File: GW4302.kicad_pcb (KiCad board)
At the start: 4 copper layers, 57.9 x 51.6 mm, 29 parts, among them J1 C64

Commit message: As submitted to JLC
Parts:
- removed the H1 at (107.7, 47.5)
- removed the H2 at (156.5, 47.5)
- removed REF**: SOT-223, stdpads:SOT-223
- removed REF** (x7): C_0603, stdpads:C_0603
- removed REF**: TSSOP-14_4.4x5mm_P0.65mm, stdpads:TSSOP-14_4.4x5mm_P0.65mm
- removed REF**: TQFP-100_14x14mm_P0.5mm, stdpads:TQFP-100_14x14mm_P0.5mm
- removed REF** (x2): TSSOP-20_4.4x6.5mm_P0.65mm, stdpads:TSSOP-20_4.4x6.5mm_P0.65mm
- added C1: 10u, stdpads:C_0805, F.Cu at (109.5, 74.8)
- added C10: 2u2, stdpads:C_0603, F.Cu at (131.3, 79.8)
- added C12: 2u2, stdpads:C_0603, F.Cu at (149.8, 79.8)
- added C13: 2u2, stdpads:C_0603, F.Cu at (112.3, 61.5)
- added C14: 2u2, stdpads:C_0603, F.Cu at (112.3, 70.0)
- added C15: 2u2, stdpads:C_0603, F.Cu at (116.5, 75.0)
- added C16: 2u2, stdpads:C_0603, F.Cu at (125.5, 75.0)
- added C17: 2u2, stdpads:C_0603, F.Cu at (128.8, 75.0)
- added C18: 2u2, stdpads:C_0603, F.Cu at (131.7, 69.0)
- added C19: 2u2, stdpads:C_0603, F.Cu at (131.7, 60.5)
- added C2: 10u, stdpads:C_0805, F.Cu at (112.6, 73.4)
- added C20: 2u2, stdpads:C_0603, F.Cu at (126.2, 55.6)
- added C21: 2u2, stdpads:C_0603, F.Cu at (119.8, 55.6)
- added C22: 2u2, stdpads:C_0603, F.Cu at (115.2, 55.6)
- added C23: 2u2, stdpads:C_0603, F.Cu at (115.8, 79.5)
- added C24: 2u2, stdpads:C_0603, F.Cu at (156.8, 72.0)
- added C25: 2u2, stdpads:C_0603, F.Cu at (156.8, 68.8)
- added C26: 2u2, stdpads:C_0603, F.Cu at (156.8, 64.8)
- added C27: 2u2, stdpads:C_0603, F.Cu at (156.8, 54.4)
- added C28: 2u2, stdpads:C_0603, F.Cu at (141.2, 64.8)
- added C29: 2u2, stdpads:C_0603, F.Cu at (141.2, 71.2)
- added C3: 10u, stdpads:C_0805, F.Cu at (106.2, 62.1)
- added C30: 2u2, stdpads:C_0603, F.Cu at (110.2, 47.0)
- added C31: 2u2, stdpads:C_0603, F.Cu at (116.7, 40.8)
- added C32: 22p, stdpads:C_0603, F.Cu at (110.0, 56.5)
- added C33: 22p, stdpads:C_0603, F.Cu at (107.4, 44.0)
- added C34: 22p, stdpads:C_0603, F.Cu at (141.4, 41.2)
- added C35: 2u2, stdpads:C_0603, F.Cu at (119.6, 41.7)
- added C36: 2u2, stdpads:C_0603, F.Cu at (146.7, 40.6)
- added C37: 2u2, stdpads:C_0603, F.Cu at (148.0, 48.6)
- added C38: 22p, stdpads:C_0603, F.Cu at (129.2, 44.8)
- added C39: 22p, stdpads:C_0603, F.Cu at (111.8, 39.3)
- added C4: 10u, stdpads:C_0805, F.Cu at (109.7, 62.1)
- added C5: 10u, stdpads:C_0805, F.Cu at (106.2, 59.9)
- added C6: 10u, stdpads:C_0805, F.Cu at (109.7, 59.9)
- added C7: 22p, stdpads:C_0603, F.Cu at (148.0, 45.6)
- added H3: , stdpads:PasteHole_1.152mm_NPTH, F.Cu at (156.5, 38.7)
- added H4: , stdpads:PasteHole_1.152mm_NPTH, F.Cu at (105.1, 41.3)
- added H5: , stdpads:PasteHole_1.152mm_NPTH, F.Cu at (158.8, 82.9)
- added J2: microUSB, stdpads:USB_Micro-B_ShouHan_MicroXNJ, F.Cu at (134.3, 39.8)
- added J3: JTAG, Connector:Tag-Connect_TC2050-IDC-FP_2x05_P1.27mm_Vertical, F.Cu at (154.7, 47.4)
- added R1: 1k, stdpads:R_0603, F.Cu at (121.7, 41.6)
- added R10: 47, stdpads:R_0603, F.Cu at (145.8, 46.4)
- added R11: 10k, stdpads:R_0603, F.Cu at (137.4, 56.0)
- added R12: 10k, stdpads:R_0603, F.Cu at (137.4, 54.5)
- added R13: 10k, stdpads:R_0603, F.Cu at (148.0, 47.1)
- added R14: 10k, stdpads:R_0603, F.Cu at (137.4, 53.0)
- added R15: 10k, stdpads:R_0603, F.Cu at (111.8, 40.9)
- added R16: 1k, stdpads:R_0603, F.Cu at (139.9, 41.2)
- added R2: 1k, stdpads:R_0603, F.Cu at (136.4, 44.4)
- added R3: 47, stdpads:R_0603, F.Cu at (144.9, 43.2)
- added R4: 10k, stdpads:R_0603, F.Cu at (108.3, 40.9)
- added R5: 1k, stdpads:R_0603, F.Cu at (115.8, 82.3)
- added R6: 47, stdpads:R_0603, F.Cu at (119.4, 75.8)
- added R7: 47, stdpads:R_0603, F.Cu at (119.4, 77.3)
- added R8: 10k, stdpads:R_0603, F.Cu at (141.2, 53.6)
- added R9: 10k, stdpads:R_0603, F.Cu at (137.4, 57.5)
- added U10: 74AHC125PW, stdpads:TSSOP-14_4.4x5mm_P0.65mm, F.Cu at (125.8, 43.5)
- added U11: 74LVC1G04GW, stdpads:SOT-353, F.Cu at (120.7, 45.0)
- added U12: 74LVC1G04GW, stdpads:SOT-353, F.Cu at (144.1, 40.5)
- added U13: CH340G, stdpads:SOIC-16_3.9mm, F.Cu at (114.9, 46.9)
- added U2: 74AHC245PW, stdpads:TSSOP-20_4.4x6.5mm_P0.65mm, F.Cu at (135.8, 82.0)
- added U3: LD1117S33, stdpads:SOT-223, F.Cu at (108.0, 69.1)
- added U5: 74AHC245PW, stdpads:TSSOP-20_4.4x6.5mm_P0.65mm, F.Cu at (124.8, 82.0)
- added U8: LCMXO2-640-TG100, stdpads:TQFP-100_14x14mm_P0.5mm, F.Cu at (122.0, 65.3)
- added Y1: 12M, stdpads:Crystal_HC49-SMD, F.Cu at (106.7, 51.5)
- C11, C8, C9: renamed from REF**; value C_0603 -> 2u2
- U1, U4: renamed from REF**; value TSSOP-20_4.4x6.5mm_P0.65mm -> 74AHC245PW
- U6: renamed from REF**; value TSSOP-14_4.4x5mm_P0.65mm -> 74AHC125PW
- U7: renamed from REF**; value SOT-353 -> 74LVC1G04GW
- U9: renamed from REF**; value TSOP-II-54_22.2x10.16mm_P0.8mm -> W9825G6KH-6
- moved U7 18.2 mm to (118.0, 79.7)
- moved FID1 8.76 mm to (105.1, 38.7)
- moved FID2 8.76 mm to (159.1, 38.7)
- moved C8 6.35 mm to (108.5, 79.8)
- moved U6 6.35 mm to (112.0, 82.0)
- moved FID3 2.54 mm to (158.8, 85.5)
- moved C9 1.75 mm to (120.4, 79.8)
- turned U9 to 90 degrees
- renumbered H4 to H1, H3 to H2
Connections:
- C11 pad 1: (no net) -> +3V3
- C11 pad 2: (no net) -> GND
- C8 pad 1: (no net) -> +3V3
- C8 pad 2: (no net) -> GND
- C9 pad 1: (no net) -> +3V3
- C9 pad 2: (no net) -> GND
- U1 pad 1: (no net) -> /ADIR
- U1 pad 10: (no net) -> GND
- U1 pad 11: (no net) -> /BA0
- U1 pad 12: (no net) -> /BA1
- U1 pad 13: (no net) -> /BA2
- U1 pad 14: (no net) -> /BA3
- U1 pad 15: (no net) -> /BA4
- U1 pad 16: (no net) -> /BA5
- U1 pad 17: (no net) -> /BA6
- U1 pad 18: (no net) -> /BA7
- U1 pad 19: (no net) -> /A~OE~
- U1 pad 2: (no net) -> /A7
- U1 pad 20: (no net) -> +3V3
- U1 pad 3: (no net) -> /A6
- U1 pad 4: (no net) -> /A5
- U1 pad 5: (no net) -> /A4
- U1 pad 6: (no net) -> /A3
- U1 pad 7: (no net) -> /A2
- U1 pad 8: (no net) -> /A1
- U1 pad 9: (no net) -> /A0
- U4 pad 1: (no net) -> /DDIR
- U4 pad 10: (no net) -> GND
- U4 pad 11: (no net) -> /BD0
- U4 pad 12: (no net) -> /BD1
- U4 pad 13: (no net) -> /BD2
- U4 pad 14: (no net) -> /BD3
- U4 pad 15: (no net) -> /BD4
- U4 pad 16: (no net) -> /BD5
- U4 pad 17: (no net) -> /BD6
- U4 pad 18: (no net) -> /BD7
- U4 pad 19: (no net) -> /D~OE~
- U4 pad 2: (no net) -> /D7
- U4 pad 20: (no net) -> +3V3
- U4 pad 3: (no net) -> /D6
- U4 pad 4: (no net) -> /D5
- U4 pad 5: (no net) -> /D4
- U4 pad 6: (no net) -> /D3
- U4 pad 7: (no net) -> /D2
- U4 pad 8: (no net) -> /D1
- U4 pad 9: (no net) -> /D0
- U6 pad 1: (no net) -> GND
- U6 pad 10: (no net) -> /DMA~OE~
- U6 pad 11: (no net) -> /~IRQ~
- U6 pad 12: (no net) -> GND
- U6 pad 13: (no net) -> /IRQ~OE~
- U6 pad 14: (no net) -> +3V3
- U6 pad 2: (no net) -> GND
- U6 pad 3: (no net) -> Net-(U6-Pad3)
- U6 pad 4: (no net) -> /RW~OE~
- U6 pad 5: (no net) -> /DMAR~W~
- U6 pad 6: (no net) -> /R~W~
- U6 pad 7: (no net) -> GND
- U6 pad 8: (no net) -> /~DMA~
- U6 pad 9: (no net) -> GND
- U7 pad 1: (no net) -> Net-(U7-Pad1)
- U7 pad 2: (no net) -> /DotClk
- U7 pad 3: (no net) -> GND
- U7 pad 4: (no net) -> Net-(R6-Pad2)
- U7 pad 5: (no net) -> +3V3
- U9 pad 1: (no net) -> +3V3
- U9 pad 10: (no net) -> /RD5
- U9 pad 11: (no net) -> /RD6
- U9 pad 12: (no net) -> GND
- U9 pad 13: (no net) -> /RD7
- U9 pad 14: (no net) -> +3V3
- U9 pad 15: (no net) -> /RDQML
- U9 pad 16: (no net) -> /R~WE~
- U9 pad 17: (no net) -> /~CAS~
- U9 pad 18: (no net) -> /~RAS~
- U9 pad 19: (no net) -> /R~CS~
- U9 pad 2: (no net) -> /RD0
- U9 pad 20: (no net) -> /RBA0
- U9 pad 21: (no net) -> /RBA1
- U9 pad 22: (no net) -> /RA10
- U9 pad 23: (no net) -> /RA0
- U9 pad 24: (no net) -> /RA1
- U9 pad 25: (no net) -> /RA2
- U9 pad 26: (no net) -> /RA3
- U9 pad 27: (no net) -> +3V3
- U9 pad 28: (no net) -> GND
- U9 pad 29: (no net) -> /RA4
- U9 pad 3: (no net) -> +3V3
- U9 pad 30: (no net) -> /RA5
- U9 pad 31: (no net) -> /RA6
- U9 pad 32: (no net) -> /RA7
- U9 pad 33: (no net) -> /RA8
- U9 pad 34: (no net) -> /RA9
- U9 pad 35: (no net) -> /RA11
- U9 pad 36: (no net) -> /RA12
- U9 pad 37: (no net) -> /RCKE
- U9 pad 38: (no net) -> /RCLK
- U9 pad 39: (no net) -> /RDQMH
- U9 pad 4: (no net) -> /RD1
- U9 pad 41: (no net) -> GND
- U9 pad 42: (no net) -> /RD7
- U9 pad 43: (no net) -> +3V3
- U9 pad 44: (no net) -> /RD6
- U9 pad 45: (no net) -> /RD5
- U9 pad 46: (no net) -> GND
- U9 pad 47: (no net) -> /RD4
- U9 pad 48: (no net) -> /RD3
- U9 pad 49: (no net) -> +3V3
- U9 pad 5: (no net) -> /RD2
- U9 pad 50: (no net) -> /RD2
- U9 pad 51: (no net) -> /RD1
- U9 pad 52: (no net) -> GND
- U9 pad 53: (no net) -> /RD0
- U9 pad 54: (no net) -> GND
- U9 pad 6: (no net) -> GND
- U9 pad 7: (no net) -> /RD3
- U9 pad 8: (no net) -> /RD4
- U9 pad 9: (no net) -> +3V3
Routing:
- net +3V3: track 0.00 -> 387.7 mm, vias 0 -> 122
- net GND: track 23.2 -> 166.8 mm, vias 48 -> 207
- net /TDO: track 0.00 -> 64.8 mm, vias 0 -> 3
- net /BD1: track 0.00 -> 59.3 mm, vias 0 -> 2
- net /BD0: track 0.00 -> 58.0 mm, vias 0 -> 2
- net /BD3: track 0.00 -> 58.0 mm, vias 0 -> 2
- net /TMS: track 0.00 -> 57.9 mm, vias 0 -> 4
- net /BD5: track 0.00 -> 56.6 mm, vias 0 -> 2
- net /BD2: track 0.00 -> 56.3 mm, vias 0 -> 2
- net /DDIR: track 0.00 -> 56.0 mm, vias 0 -> 2
- net /D~OE~: track 0.00 -> 56.0 mm, vias 0 -> 2
- net /BD4: track 0.00 -> 55.7 mm, vias 0 -> 2
- net /RA3: track 0.00 -> 55.5 mm
- net /BD7: track 0.00 -> 55.3 mm, vias 0 -> 2
- net /RA2: track 0.00 -> 54.6 mm
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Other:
- board size 57.9 x 51.6 mm -> 57.9 x 60.3 mm
- board text added: "JLCJLCJLCJLC"

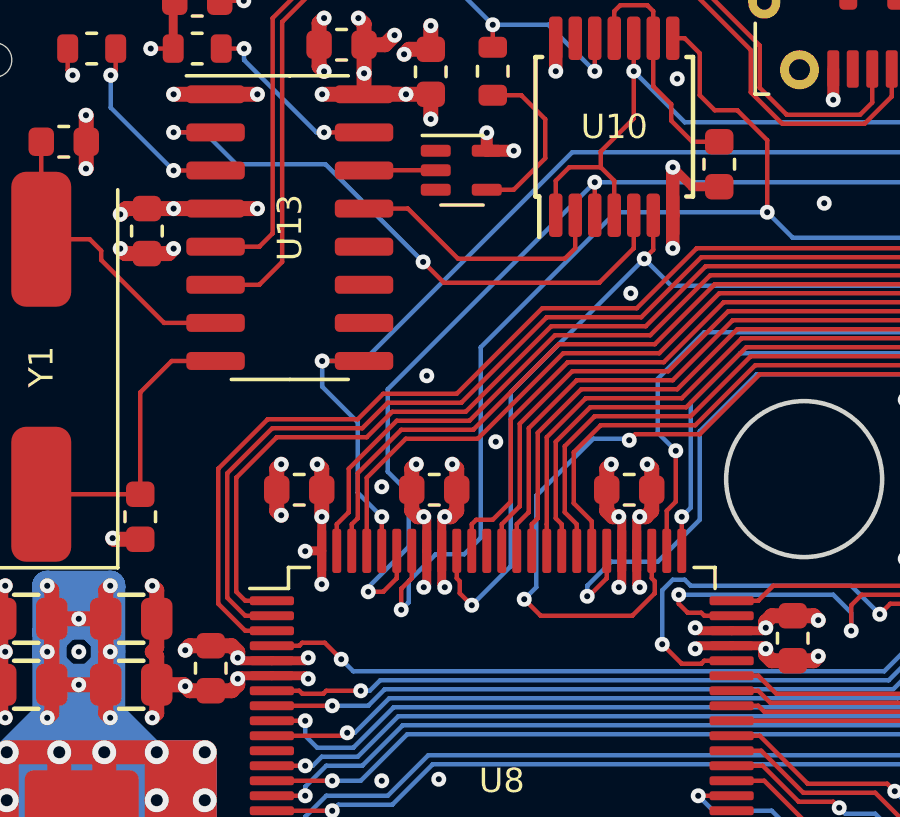
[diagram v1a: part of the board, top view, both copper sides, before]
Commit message: Fix JTAG connections on board
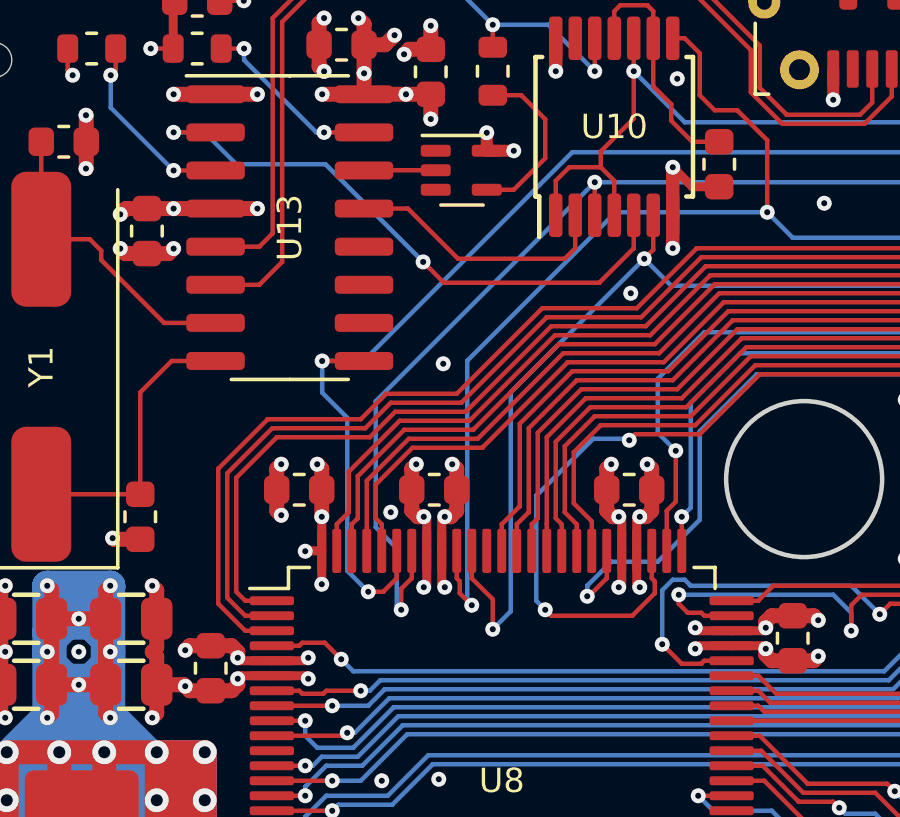
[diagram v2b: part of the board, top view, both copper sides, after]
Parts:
- U11, U12: value 74LVC1G04GW -> 74AHC1G04GW
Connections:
- U8 pad 28: Net-(U8-Pad28) -> /B~RESET~
- U8 pad 90: /RBA0 -> /TMS
- U8 pad 91: /TMS -> /TCKr
- U8 pad 94: /TCKr -> /TDI
- U8 pad 95: /TDI -> /TDO
- U8 pad 96: /TDO -> /RBA0
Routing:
- net /TDO: track 64.8 -> 68.0 mm
- net /RBA0: track 44.2 -> 46.6 mm
- net /TCKr: track 49.9 -> 48.3 mm
- net /TMS: track 57.9 -> 59.3 mm
- net /RA5: track 34.2 -> 33.6 mm
- net GND: vias 207 -> 206

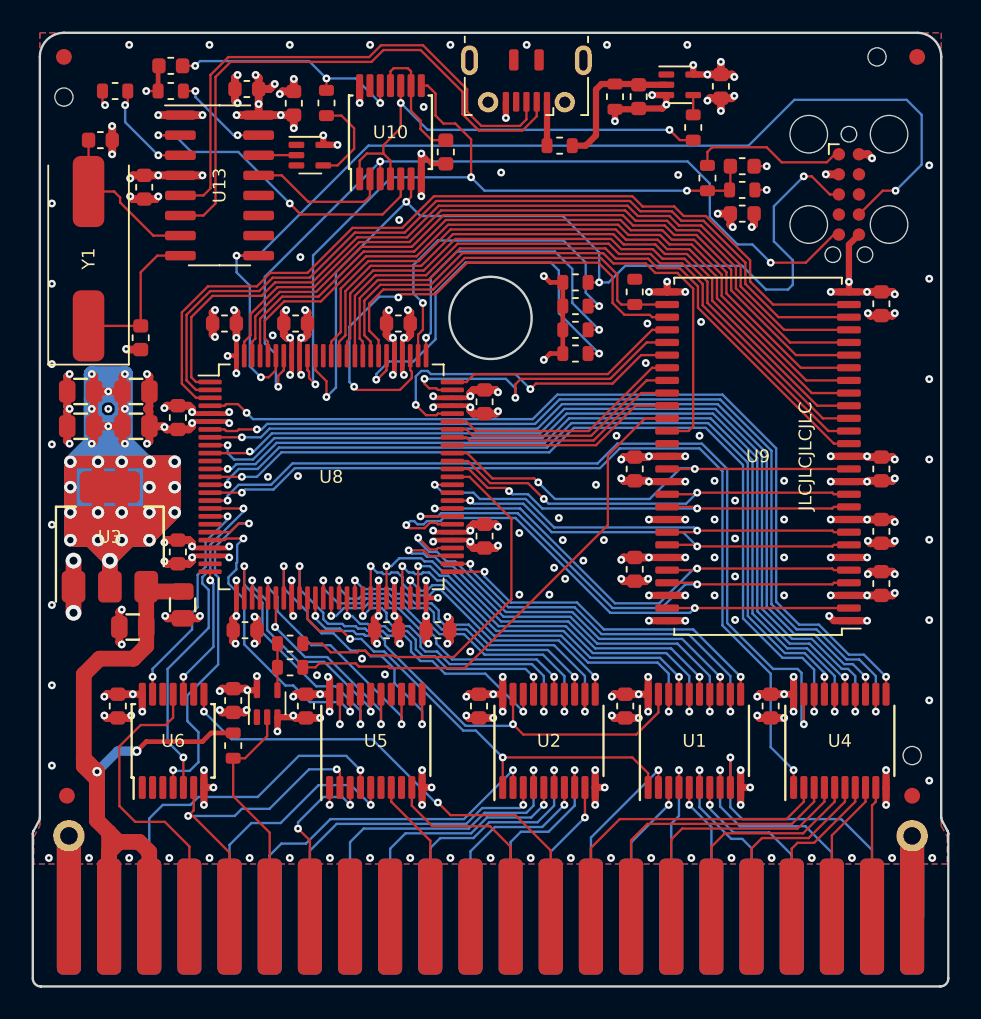
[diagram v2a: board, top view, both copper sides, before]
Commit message: Migrate to KiCAD 6
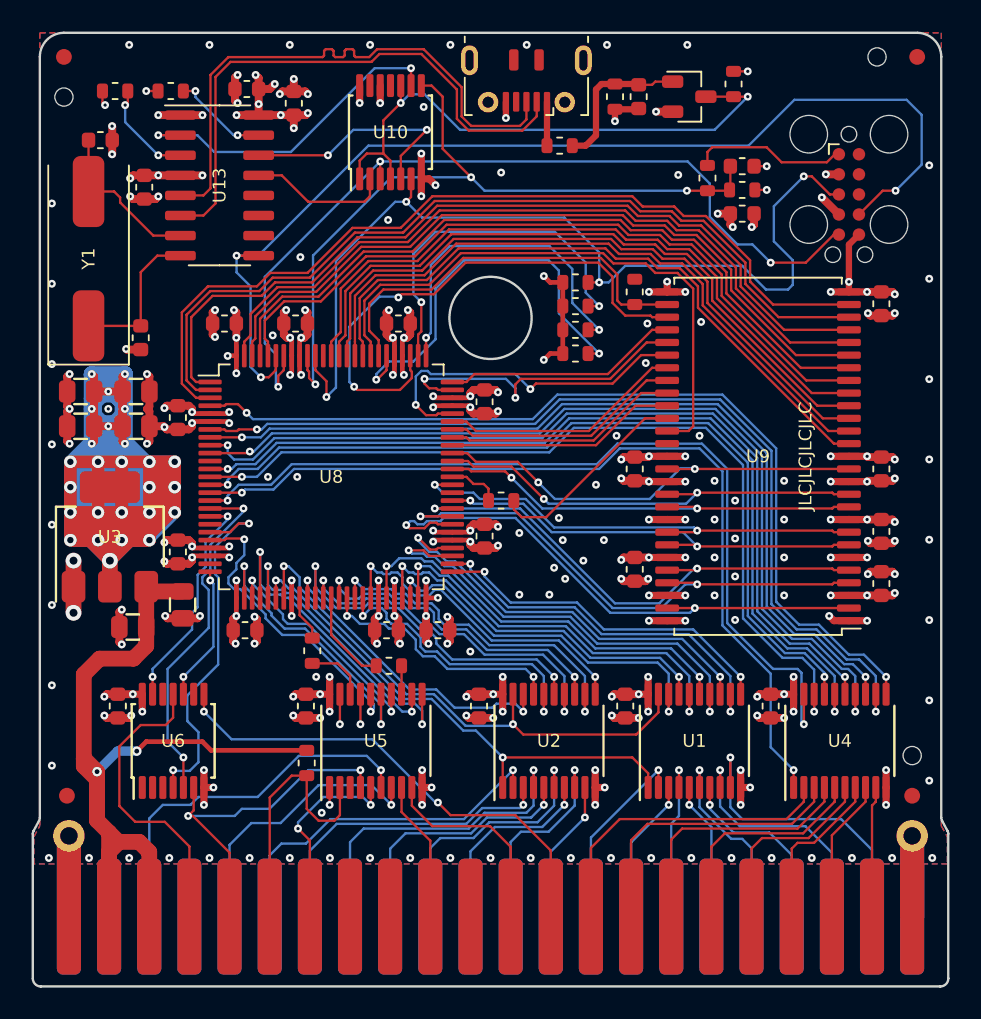
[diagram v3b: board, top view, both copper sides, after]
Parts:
- removed the C23 at (115.8, 79.5)
- removed C36, C37: 2u2, stdpads:C_0603
- removed C38, C39: 22p, stdpads:C_0603
- removed U11, U12: 74AHC1G04GW, stdpads:SOT-353
- removed U7: 74LVC1G04GW, stdpads:SOT-353
- added C35: 2u2, stdpads:C_0603, F.Cu at (148.0, 48.6)
- added Q1: 2N3904, stdpads:SOT-23, F.Cu at (144.7, 41.2)
- R1: value 1k -> 47
- R3: value 47 -> 1k
- moved R1 35.8 mm to (125.7, 77.2), turned to 0 degrees
- moved R7 17.0 mm to (132.8, 66.8)
- moved R5 4.78 mm to (120.5, 83.4)
- moved R3 3.75 mm to (147.4, 40.5), turned to -90 degrees
- moved R6 1.47 mm to (120.8, 76.3), turned to -90 degrees
- renumbered C35 to C23
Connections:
- net /DMAR~W~ renamed /DMAR~{W}
- net /DMA~OE~ renamed /DMA~{OE}
- net /D~OE~ renamed /D~{OE}
- net /IRQ~OE~ renamed /IRQ~{OE}
- net /RESET~OE~ renamed /RESET~{OE}
- net /RW~OE~ renamed /RW~{OE}
- net /R~CS~ renamed /R~{CS}
- net /R~WE~ renamed /R~{WE}
- net /~CAS~ renamed /~{CAS}
- net /~DMA~ renamed /~{DMA}
- net /~EXROM~ renamed /~{EXROM}
- net /~GAME~ renamed /~{GAME}
- net /~INIT~ renamed /~{INIT}
- net /~IRQ~ renamed /~{IRQ}
- net /~NMI~ renamed /~{NMI}
- net /~PROG~ renamed /~{PROG}
- net /~RAS~ renamed /~{RAS}
- net /~ROMH~ renamed /~{ROMH}
- net /~ROML~ renamed /~{ROML}
- J1 pad 10: /~IO2~ -> /~{IO2}
- J1 pad 42: /~RESET~ -> /~{RESET}
- J1 pad 5: /R~W~ -> /R~{W}
- J1 pad 7: /~IO1~ -> /~{IO1}
- J2 pad 4: Net-(J2-Pad4) -> unconnected-(J2-Pad4)
- J3 pad 10: Net-(J3-Pad10) -> unconnected-(J3-Pad10)
- J3 pad 8: Net-(J3-Pad8) -> unconnected-(J3-Pad8)
- J3 pad 9: Net-(J3-Pad9) -> unconnected-(J3-Pad9)
- R1 pad 1: /UTCK -> /BPHI2
- R3 pad 1: /JTAG~OE~ -> +3V3
- R3 pad 2: Net-(R3-Pad2) -> /JTAG~{OE}
- R6 pad 1: /ACLK -> /C8M
- R7 pad 2: Net-(R6-Pad2) -> Net-(R7-Pad2)
- U1 pad 19: /A~OE~ -> /A~{OE}
- U10 pad 1: /JTAG~OE~ -> /JTAG~{OE}
- U10 pad 10: /JTAG~OE~ -> /JTAG~{OE}
- U10 pad 11: /UTCKb -> unconnected-(U10-Pad11)
- U10 pad 12: /UTCK -> GND
- U10 pad 4: /JTAG~OE~ -> /JTAG~{OE}
- U10 pad 9: /UTCKb -> /UTCK
- U13 pad 10: Net-(U13-Pad10) -> unconnected-(U13-Pad10)
- U13 pad 11: Net-(U13-Pad11) -> unconnected-(U13-Pad11)
- U13 pad 12: Net-(U13-Pad12) -> unconnected-(U13-Pad12)
- U13 pad 14: /U~TCK~ -> /UTMS
- U13 pad 2: /UTMS -> /UTCK
- U2 pad 19: /A~OE~ -> /A~{OE}
- U5 pad 12: Net-(U5-Pad12) -> /B~{IO2}
- U5 pad 13: /B~IO2~ -> Net-(R1-Pad2)
- U5 pad 14: Net-(U5-Pad14) -> /B~{RESET}
- U5 pad 15: /BPHI2 -> /B~{IO1}
- U5 pad 16: /B~RESET~ -> /BR~{W}
- U5 pad 17: /B~IO1~ -> GND
- U5 pad 18: /BR~W~ -> Net-(R6-Pad2)
- U5 pad 2: /R~W~ -> /DotClk
- U5 pad 3: /~IO1~ -> GND
- U5 pad 4: /~RESET~ -> /R~{W}
- U5 pad 5: /PHI2 -> /~{IO1}
- U5 pad 6: GND -> /~{RESET}
- U5 pad 7: /~IO2~ -> /PHI2
- U5 pad 8: GND -> /~{IO2}
- U6 pad 3: Net-(U6-Pad3) -> unconnected-(U6-Pad3)
- U6 pad 6: /R~W~ -> /R~{W}
- U8 pad 21: /BR~W~ -> /BR~{W}
- U8 pad 24: Net-(U8-Pad24) -> unconnected-(U8-Pad24)
- U8 pad 27: /B~IO1~ -> /B~{IO1}
- U8 pad 28: /B~RESET~ -> /B~{RESET}
- U8 pad 29: Net-(U8-Pad29) -> /B~{IO2}
- U8 pad 30: /B~IO2~ -> /BBA
- U8 pad 31: /BPHI2 -> /ADIR
- U8 pad 32: /BBA -> /A~{OE}
- U8 pad 34: /BA15 -> /C8M
- U8 pad 35: /ADIR -> /BA15
- U8 pad 36: /A~OE~ -> /BA12
- U8 pad 38: /BA12 -> /BPHI2
- U8 pad 63: /ACLK -> Net-(R7-Pad2)
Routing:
- net /JTAG~{OE}: track 0.00 -> 36.0 mm, vias 0 -> 2
- net /A~{OE}: track 0.00 -> 34.2 mm, vias 0 -> 2
- net /A~OE~: track 29.9 -> 0.00 mm, vias 2 -> 0
- net /JTAG~OE~: track 28.9 -> 0.00 mm, vias 2 -> 0
- net /ACLK: track 25.1 -> 0.00 mm
- net /~{RESET}: track 0.00 -> 23.4 mm, vias 0 -> 1
- net /R~{W}: track 0.00 -> 22.8 mm, vias 0 -> 2
- net /~RESET~: track 22.1 -> 0.00 mm, vias 1 -> 0
- net /R~W~: track 21.4 -> 0.00 mm, vias 2 -> 0
- net /BR~{W}: track 0.00 -> 19.6 mm, vias 0 -> 2
- net /BR~W~: track 19.2 -> 0.00 mm, vias 2 -> 0
- net /RCLK: track 32.4 -> 13.2 mm
- net /B~{IO2}: track 0.00 -> 19.0 mm, vias 0 -> 2
- net /B~{IO1}: track 0.00 -> 18.3 mm, vias 0 -> 2
- net /B~IO1~: track 17.7 -> 0.00 mm, vias 2 -> 0
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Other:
- net class Default removed

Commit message: RFC
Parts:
- removed Q1: 2N3904, stdpads:SOT-23
- R15, R4: value 10k -> 1k
- R16: value 1k -> 10k
- moved R3 25.3 mm to (122.2, 41.6), turned to 90 degrees
- moved R6 0.20 mm to (120.6, 76.3)
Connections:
- R3 pad 1: +3V3 -> /JTAG~{OE}
- R3 pad 2: /JTAG~{OE} -> GND
- U10 pad 11: unconnected-(U10-Pad11) -> /JTAG~{OE}
- U10 pad 12: GND -> +3V3
- U10 pad 13: GND -> Net-(C34-Pad1)
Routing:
- net /JTAG~{OE}: track 36.0 -> 14.4 mm, vias 2 -> 0
- net Net-(C34-Pad1): track 9.77 -> 29.7 mm, vias 0 -> 2
- net /TMS: track 59.7 -> 56.1 mm
- net /RCLK: track 13.2 -> 11.9 mm
- net Net-(C32-Pad1): track 9.64 -> 8.78 mm
- net /~{IRQ}: track 19.3 -> 18.8 mm
- net GND: track 159.1 -> 158.7 mm, vias 203 -> 272
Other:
- board text added: "16 MB REU"
- board text added: "4302A"
- board text added: "GW"
- board text added: "Garrett’s Workshop"
- board text added: "for C64"
